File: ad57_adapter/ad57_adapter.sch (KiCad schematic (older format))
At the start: 8 parts

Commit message: added a pdf schematic plot
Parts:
- added J8: Screw_Terminal_01x06, symbol Connector:Screw_Terminal_01x06
- J1: renamed from J?; LCSC (none) -> https://www.reichelt.de/leiterplattenklemme-2-polig-rm-2-54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
- J2: renamed from J?; LCSC (none) -> https://www.reichelt.de/leiterplattenklemme-6-polig-rm-2-54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
- gave numbers to parts that had none: 6
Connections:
- net BZZOUT1: now also J8.4 (Pin_4)
- net BZZOUT2: now also J8.5 (Pin_5)
- net GND: now also J8.6 (Pin_6)
- net EN2: now reaches J6.4
- net EN2: now also J8.3 (Pin_3)
- net +12V renamed VIN
- net VIN: now also J8.1 (Pin_1)
- net EN renamed EN1
- net EN1: now also J8.2 (Pin_2)
- no-connect marks 5 -> 4
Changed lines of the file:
@@
 encoding utf-8
 Sheet 1 1
-Title ""
-Date ""
-Rev ""
+Title "AD57 Adapter PCB"
+Date "2021-01-30"
+Rev "0.1"
 Comp ""
 Comment1 ""
@@
 $EndDescr
 $Comp
-L Connector:DB15_Female_HighDensity J?
+L Connector:DB15_Female_HighDensity J5
 U 1 1 60152F5A
 P 4425 1900
-F 0 "J?" H 4425 2767 50  0000 C CNN
+F 0 "J5" H 4425 2767 50  0000 C CNN
 F 1 "DB15_Female_HighDensity" H 4425 2676 50  0000 C CNN
 F 2 "" H 3475 2300 50  0001 C CNN
@@
 $EndComp
 $Comp
-L Connector:DB15_Female_HighDensity J?
+L Connector:DB15_Female_HighDensity J6
 U 1 1 60154BF6
 P 4475 3450
-F 0 "J?" H 4475 4317 50  0000 C CNN
+F 0 "J6" H 4475 4317 50  0000 C CNN
 F 1 "DB15_Female_HighDensity" H 4475 4226 50  0000 C CNN
 F 2 "" H 3525 3850 50  0001 C CNN
@@
 $EndComp
 $Comp
-L Connector:RJ45 J?
+L Connector:RJ45 J7
 U 1 1 60155F2E
 P 6450 2325
-F 0 "J?" H 6507 2992 50  0000 C CNN
+F 0 "J7" H 6507 2992 50  0000 C CNN
 F 1 "RJ45_CAN" H 6507 2901 50  0000 C CNN
 F 2 "" V 6450 2350 50  0001 C CNN
@@
 	1    0    0    -1
 $EndComp
-$Comp
-L Connector:Screw_Terminal_01x02 J?
-U 1 1 601581C2
-P 1950 1600
-F 0 "J?" H 2030 1592 50  0000 L CNN
-F 1 "Screw_Terminal_01x02" H 2030 1501 50  0000 L CNN
-F 2 "" H 1950 1600 50  0001 C CNN
-F 3 "~" H 1950 1600 50  0001 C CNN
-	1    1950 1600
-	1    0    0    -1
-$EndComp
 Text Notes 1900 1500 0    50   ~ 0
 12V
-$Comp
-L power:+12V #PWR?
-U 1 1 6015928A
-P 1750 1600
-F 0 "#PWR?" H 1750 1450 50  0001 C CNN
-F 1 "+12V" H 1765 1773 50  0000 C CNN
-F 2 "" H 1750 1600 50  0001 C CNN
-F 3 "" H 1750 1600 50  0001 C CNN
-	1    1750 1600
-	1    0    0    -1
-$EndComp
-$Comp
-L power:GND #PWR?
-U 1 1 60159DB4
-P 1750 1700
-F 0 "#PWR?" H 1750 1450 50  0001 C CNN
-F 1 "GND" H 1755 1527 50  0000 C CNN
-F 2 "" H 1750 1700 50  0001 C CNN
-F 3 "" H 1750 1700 50  0001 C CNN
-	1    1750 1700
-	1    0    0    -1
-$EndComp
 Text Notes 3775 1725 3    50   ~ 0
 Top - Connector 1
@@
 Wire Wire Line
 	1600 1600 1750 1600
-Connection ~ 1750 1600
 Text GLabel 4825 1600 1    50   Input ~ 0
 VIN
@@
 Wire Wire Line
 	1600 1700 1750 1700
-Connection ~ 1750 1700
 Text GLabel 4075 3150 1    50   Input ~ 0
 GND
@@
 DOUT2
 Text GLabel 4225 1600 1    50   Input ~ 0
-EN
-NoConn ~ 4275 3150
+EN1
 Text GLabel 4375 3150 1    50   Input ~ 0
 DOUT3
@@
 BZZOUT2
 $Comp
-L Jumper:SolderJumper_2_Open JP?
+L Jumper:SolderJumper_2_Open JP1
 U 1 1 6016FD9F
 P 6550 3300
-F 0 "JP?" H 6550 3505 50  0000 C CNN
+F 0 "JP1" H 6550 3505 50  0000 C CNN
 F 1 "CAN_Termination" H 6550 3414 50  0000 C CNN
 F 2 "" H 6550 3300 50  0001 C CNN
@@
 RXD2
 $Comp
-L Connector:Screw_Terminal_01x06 J?
+L Connector:Screw_Terminal_01x06 J2
 U 1 1 60179747
 P 1950 2300
-F 0 "J?" H 2030 2292 50  0000 L CNN
+F 0 "J2" H 2030 2292 50  0000 L CNN
 F 1 "Screw_Terminal_01x06" H 2030 2201 50  0000 L CNN
 F 2 "" H 1950 2300 50  0001 C CNN
 F 3 "~" H 1950 2300 50  0001 C CNN
+F 4 "https://www.reichelt.de/leiterplattenklemme-6-polig-rm-2-54-mm-dg308-2-54-6-p276218.html?&trstct=pos_2&nbc=1" H 1950 2300 50  0001 C CNN "LCSC"
 	1    1950 2300
 	1    0    0    -1
@@
 GND
 $Comp
-L Connector:Screw_Terminal_01x06 J?
+L Connector:Screw_Terminal_01x06 J3
 U 1 1 6017BCBD
 P 1950 3075
-F 0 "J?" H 2030 3067 50  0000 L CNN
+F 0 "J3" H 2030 3067 50  0000 L CNN
 F 1 "Screw_Terminal_01x06" H 2030 2976 50  0000 L CNN
 F 2 "" H 1950 3075 50  0001 C CNN
@@
 GND
 $Comp
-L Connector:Screw_Terminal_01x06 J?
+L Connector:Screw_Terminal_01x06 J4
 U 1 1 6017CC42
 P 1950 3850
-F 0 "J?" H 2030 3842 50  0000 L CNN
+F 0 "J4" H 2030 3842 50  0000 L CNN
 F 1 "Screw_Terminal_01x06" H 2030 3751 50  0000 L CNN
 F 2 "" H 1950 3850 50  0001 C CNN
@@
 Text GLabel 1750 3650 0    50   Input ~ 0
 VIN
+$Comp
+L Connector:Screw_Terminal_01x06 J8
+U 1 1 60182996
+P 1950 4675
+F 0 "J8" H 2030 4667 50  0000 L CNN
+F 1 "Screw_Terminal_01x06" H 2030 4576 50  0000 L CNN
+F 2 "" H 1950 4675 50  0001 C CNN
+F 3 "~" H 1950 4675 50  0001 C CNN
+	1    1950 4675
+	1    0    0    -1
+$EndComp
+Text GLabel 1750 4575 0    50   Input ~ 0
+EN1
+Text GLabel 1750 4775 0    50   Input ~ 0
+BZZOUT1
+Text GLabel 1750 4875 0    50   Input ~ 0
+BZZOUT2
+Text GLabel 4275 3150 1    50   Input ~ 0
+EN2
+Text GLabel 1750 4675 0    50   Input ~ 0
+EN2
+Text GLabel 1750 4975 0    50   Input ~ 0
+GND
+Text GLabel 1750 4475 0    50   Input ~ 0
+VIN
+$Comp
+L Connector:Screw_Terminal_01x02 J1
+U 1 1 601581C2
+P 1950 1600
+F 0 "J1" H 2030 1592 50  0000 L CNN
+F 1 "Screw_Terminal_01x02" H 2030 1501 50  0000 L CNN
+F 2 "" H 1950 1600 50  0001 C CNN
+F 3 "~" H 1950 1600 50  0001 C CNN
+F 4 "https://www.reichelt.de/leiterplattenklemme-2-polig-rm-2-54-mm-dg308-2-54-2-p276214.html?&trstct=pos_6&nbc=1" H 1950 1600 50  0001 C CNN "LCSC"
+	1    1950 1600
+	1    0    0    -1
+$EndComp
 $EndSCHEMATC

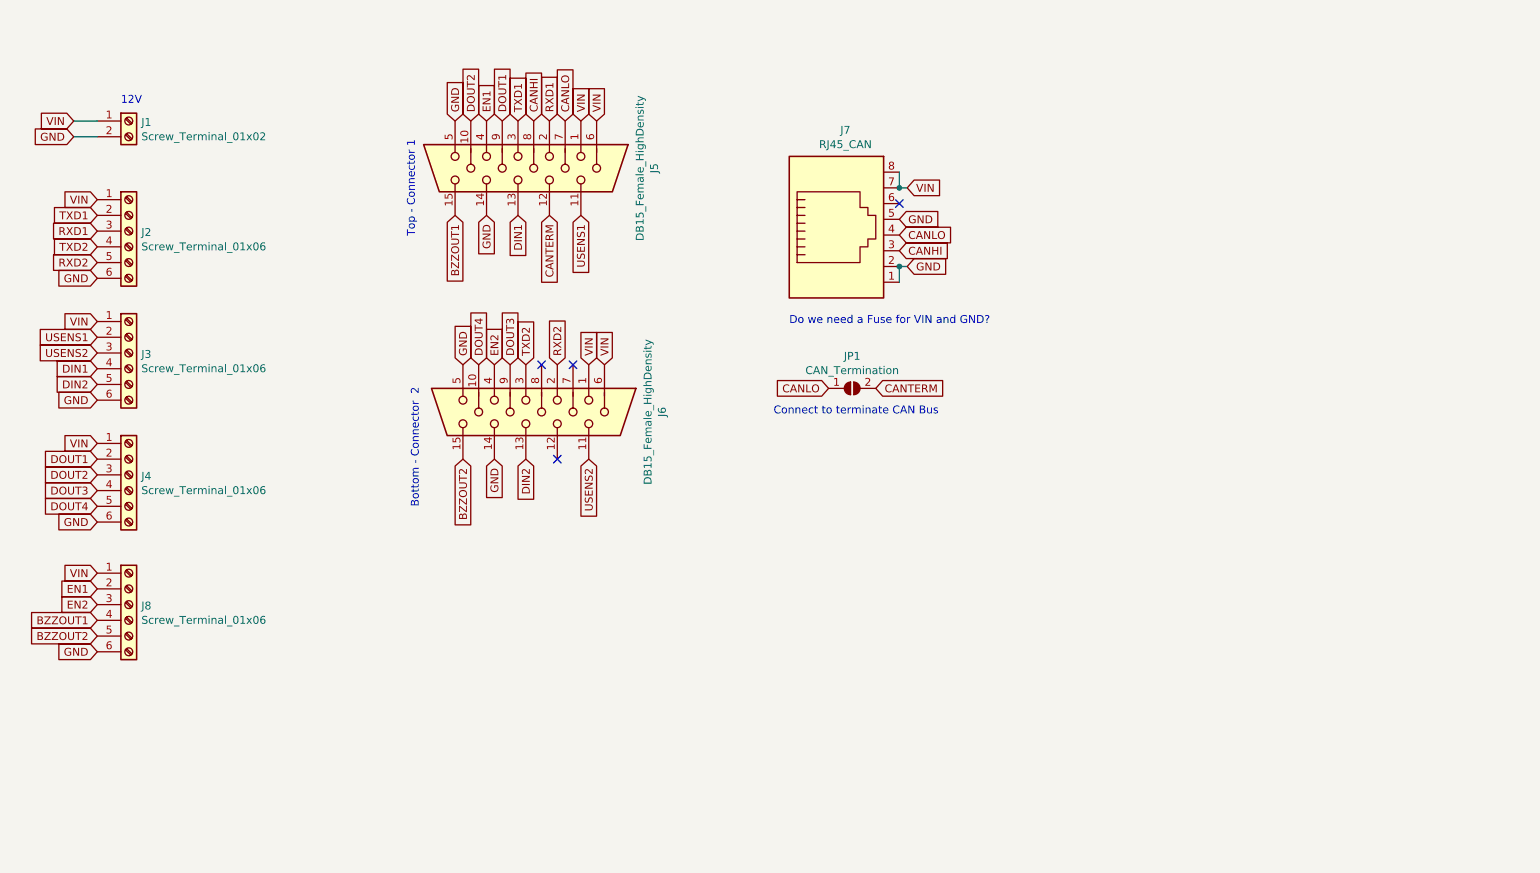
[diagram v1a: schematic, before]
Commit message: intial creation of pcb and updated schematic.
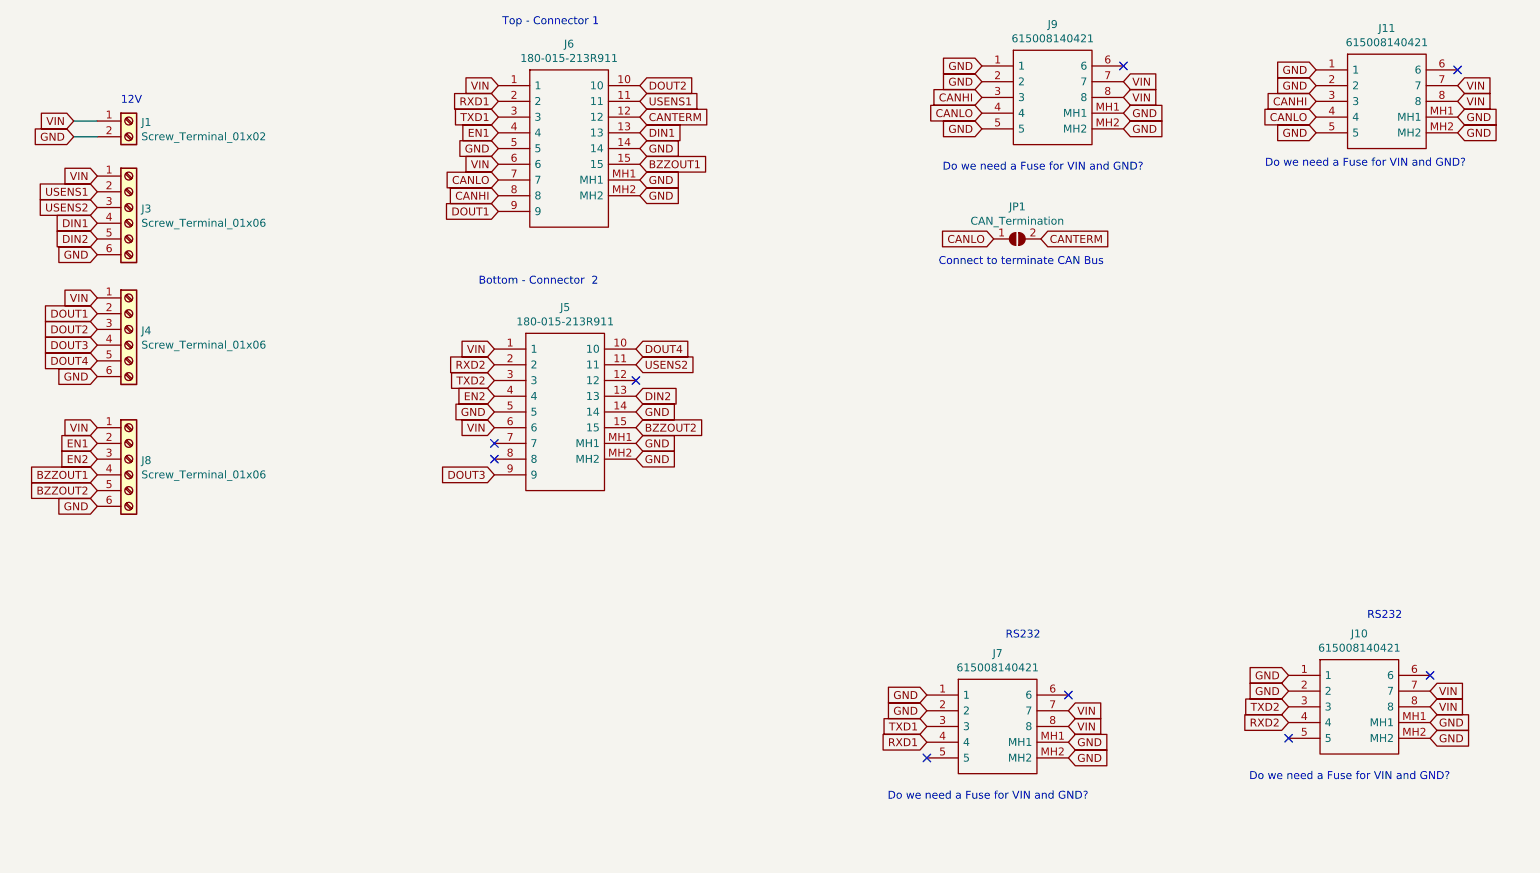
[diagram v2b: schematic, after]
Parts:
- removed J2: Screw_Terminal_01x06, symbol Connector:Screw_Terminal_01x06
- removed J5, J6: DB15_Female_HighDensity, symbol Connector:DB15_Female_HighDensity
- removed J7: RJ45_CAN, symbol Connector:RJ45
- added J10, J11, J7, J9: 615008140421, 615008140421, symbol SamacSys_Parts:615008140421
- added J5, J6: 180-015-213R911, 180015213R911, symbol SamacSys_Parts:180-015-213R911
- J1: footprint (none) -> TerminalBlock_TE-Connectivity:TerminalBlock_TE_282834-2_1x02_P2.54mm_Horizontal
- J3, J4, J8: footprint (none) -> TerminalBlock_TE-Connectivity:TerminalBlock_TE_282834-6_1x06_P2.54mm_Horizontal
- JP1: footprint (none) -> Jumper:SolderJumper-2_P1.3mm_Open_Pad1.0x1.5mm
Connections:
- net BZZOUT1: now also J6.15
- net BZZOUT2: now also J5.15
- net CANHI: now also J11.3, J6.8, J9.3
- net CANLO: now also J11.4, J6.7, J9.4
- net CANTERM: now also J6.12
- net DIN1: now also J6.13
- net DIN2: now also J5.13
- net DOUT1: now also J6.9
- net DOUT2: now also J6.10
- net DOUT3: now also J5.9
- net DOUT4: now also J5.10
- net EN1: now also J6.4
- net EN2: now also J5.4
- net GND: now also J10.1, J10.2, J10.MH1, J10.MH2, J11.1, J11.2, J11.5, J11.MH1, J11.MH2, J5.14, J5.5, J5.MH1, J5.MH2, J6.14, J6.5, J6.MH1, J6.MH2, J7.1, J7.2, J7.MH1, J7.MH2, J9.1, J9.2, J9.5, J9.MH1, J9.MH2
- net RXD1: now also J6.2, J7.4
- net RXD2: now also J10.4, J5.2
- net TXD1: now also J6.3, J7.3
- net TXD2: now also J10.3, J5.3
- net USENS1: now also J6.11
- net USENS2: now also J5.11
- net VIN: now also J10.7, J10.8, J11.7, J11.8, J5.1, J5.6, J6.1, J6.6, J7.7, J7.8, J9.7, J9.8
- no-connect marks 4 -> 9
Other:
- note added: "RS232"
- moved on the sheet: J3, J4, J8, JP1

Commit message: generated gerber. Schematic PDF export,  3D-View immages.
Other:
- note added: "AD57 Bottom - Connector 2"
- note added: "AD57 Top - Connector 1"
- note added: "CAN RJ45"
- note added: "RS232 RJ45"
- note removed: "Bottom - Connector 2"
- note removed: "Do we need a Fuse for VIN and GND?"
- note removed: "RS232"
- note removed: "Top - Connector 1"
- moved on the sheet: J1, J10, J11, J3, J4, J5, J6, J7, J8, J9, JP1
